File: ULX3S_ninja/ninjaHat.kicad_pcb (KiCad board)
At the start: 2 copper layers, 31.8 x 55.9 mm, 2 parts, among them J1 DVI-HX-107DIP, P1 ULX3S connector (JP1)

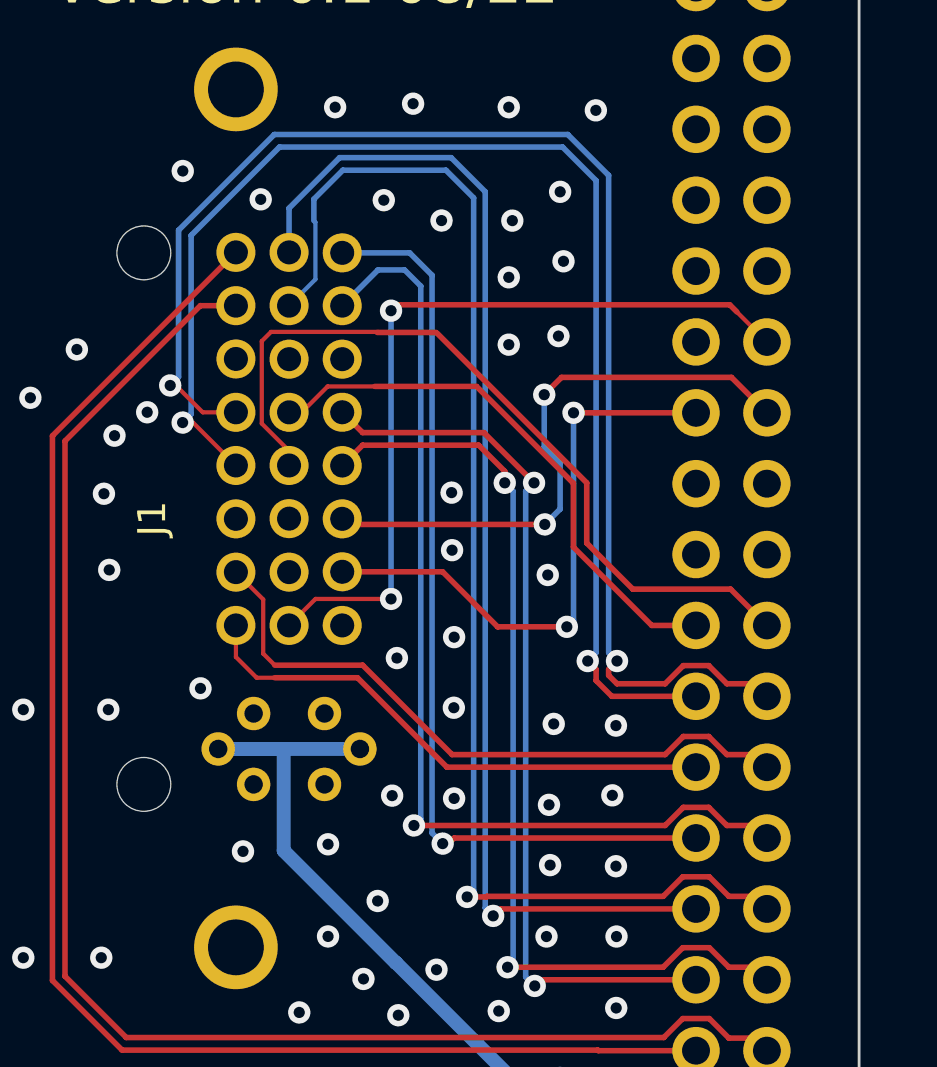
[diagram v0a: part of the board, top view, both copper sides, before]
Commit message: Changed some tracks' width to 0,2mm
was 0,152mm before. Also took a overview over PCB. looks good so far
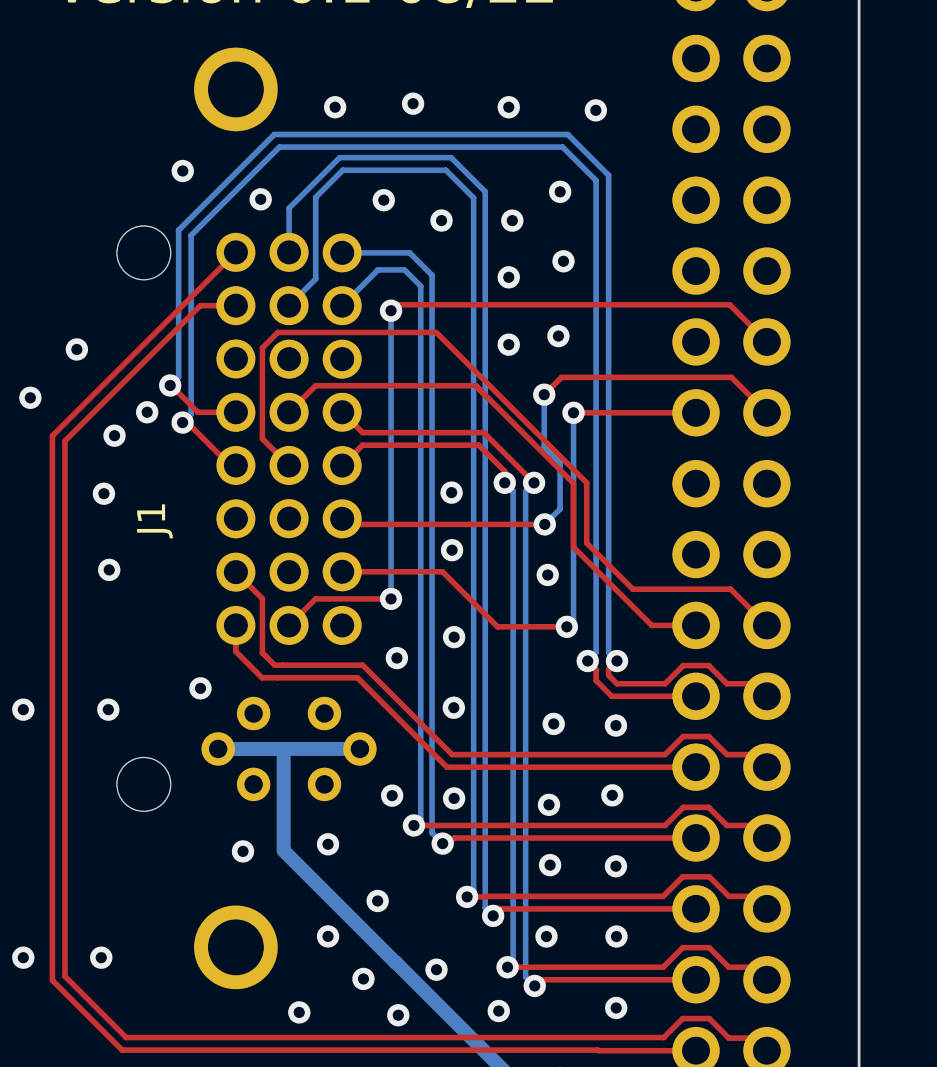
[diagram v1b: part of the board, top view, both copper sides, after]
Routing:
- net /CAM1_SDA: track 28.7 -> 29.9 mm

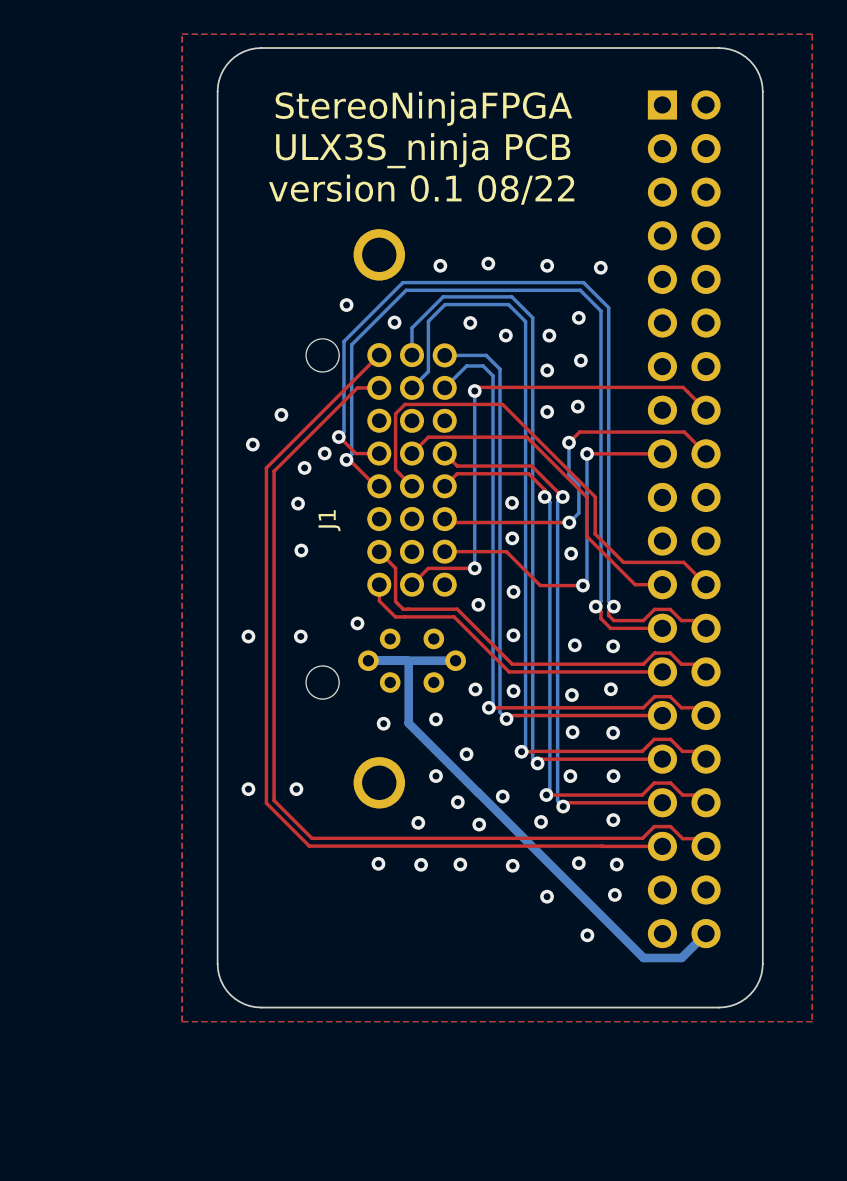
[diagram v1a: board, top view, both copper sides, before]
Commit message: PCB work and pin mapping changed
Did a first PCB layout
changed the pin mapping towards FPGAs four easier routing, schematic need to be rechecked!
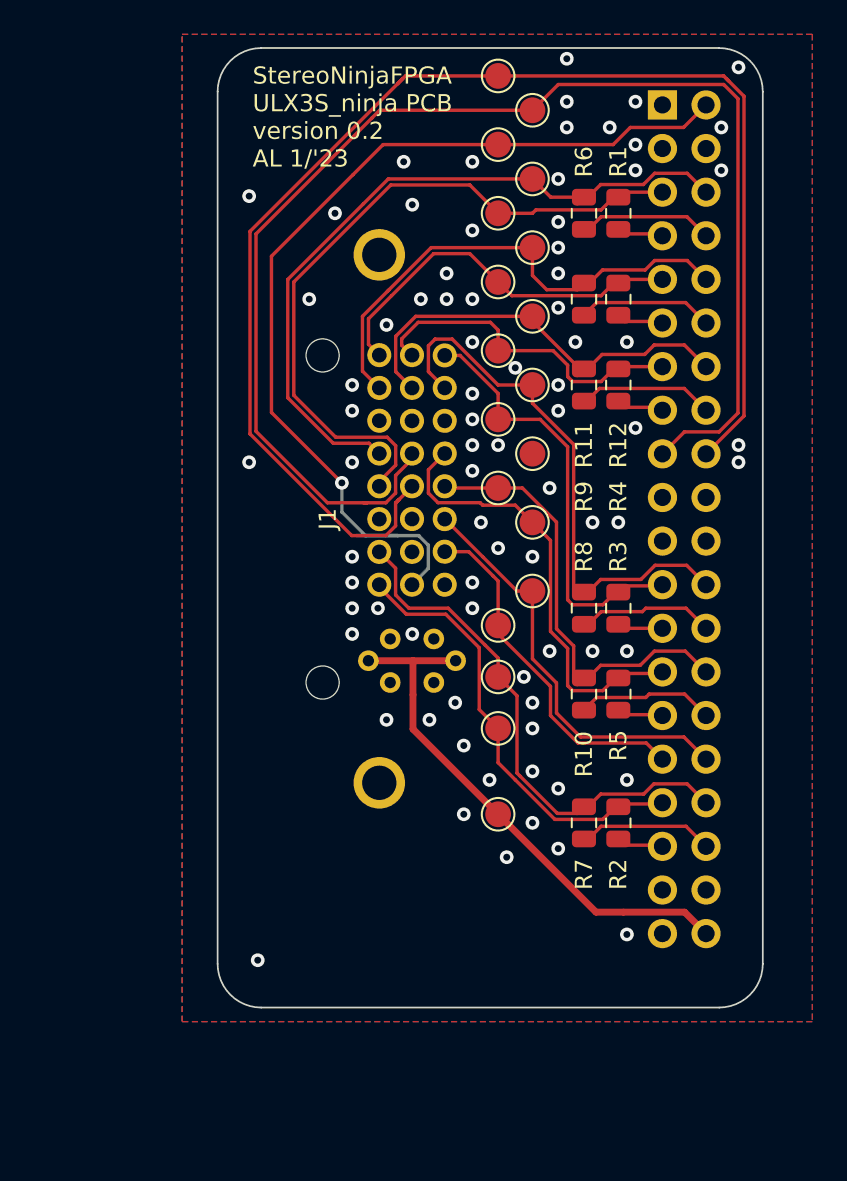
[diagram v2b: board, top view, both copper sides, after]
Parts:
- added R1: 50R, Resistor_SMD:R_0805_2012Metric, F.Cu at (219.0, 103.0)
- added R10: 50R, Resistor_SMD:R_0805_2012Metric, F.Cu at (217.0, 131.0)
- added R11: 50R, Resistor_SMD:R_0805_2012Metric, F.Cu at (217.0, 108.0)
- added R12: 50R, Resistor_SMD:R_0805_2012Metric, F.Cu at (219.0, 108.0)
- added R2: 50R, Resistor_SMD:R_0805_2012Metric, F.Cu at (219.0, 138.5)
- added R3: 50R, Resistor_SMD:R_0805_2012Metric, F.Cu at (219.0, 126.0)
- added R4: 50R, Resistor_SMD:R_0805_2012Metric, F.Cu at (219.0, 113.0)
- added R5: 50R, Resistor_SMD:R_0805_2012Metric, F.Cu at (219.0, 131.0)
- added R6: 50R, Resistor_SMD:R_0805_2012Metric, F.Cu at (217.0, 103.0)
- added R7: 50R, Resistor_SMD:R_0805_2012Metric, F.Cu at (217.0, 138.5)
- added R8: 50R, Resistor_SMD:R_0805_2012Metric, F.Cu at (217.0, 126.0)
- added R9: 50R, Resistor_SMD:R_0805_2012Metric, F.Cu at (217.0, 113.0)
- added TP1: TestPoint, TestPoint:TestPoint_Pad_D1.5mm, F.Cu at (212.0, 107.0)
- added TP10: TestPoint, TestPoint:TestPoint_Pad_D1.5mm, F.Cu at (212.0, 103.0)
- added TP11: TestPoint, TestPoint:TestPoint_Pad_D1.5mm, F.Cu at (212.0, 119.0)
- added TP12: TestPoint, TestPoint:TestPoint_Pad_D1.5mm, F.Cu at (212.0, 95.0)
- added TP13: TestPoint, TestPoint:TestPoint_Pad_D1.5mm, F.Cu at (214.0, 125.0)
- added TP14: TestPoint, TestPoint:TestPoint_Pad_D1.5mm, F.Cu at (212.0, 130.0)
- added TP15: TestPoint, TestPoint:TestPoint_Pad_D1.5mm, F.Cu at (212.0, 127.0)
- added TP16: TestPoint, TestPoint:TestPoint_Pad_D1.5mm, F.Cu at (212.0, 133.0)
- added TP17: TestPoint, TestPoint:TestPoint_Pad_D1.5mm, F.Cu at (212.0, 99.0)
- added TP18: TestPoint, TestPoint:TestPoint_Pad_D1.5mm, F.Cu at (214.0, 117.0)
- added TP19: TestPoint, TestPoint:TestPoint_Pad_D1.5mm, F.Cu at (212.0, 138.0)
- added TP2: TestPoint, TestPoint:TestPoint_Pad_D1.5mm, F.Cu at (212.0, 115.0)
- added TP3: TestPoint, TestPoint:TestPoint_Pad_D1.5mm, F.Cu at (212.0, 111.0)
- added TP4: TestPoint, TestPoint:TestPoint_Pad_D1.5mm, F.Cu at (214.0, 105.0)
- added TP5: TestPoint, TestPoint:TestPoint_Pad_D1.5mm, F.Cu at (214.0, 113.0)
- added TP6: TestPoint, TestPoint:TestPoint_Pad_D1.5mm, F.Cu at (214.0, 109.0)
- added TP7: TestPoint, TestPoint:TestPoint_Pad_D1.5mm, F.Cu at (214.0, 101.0)
- added TP8: TestPoint, TestPoint:TestPoint_Pad_D1.5mm, F.Cu at (214.0, 121.0)
- added TP9: TestPoint, TestPoint:TestPoint_Pad_D1.5mm, F.Cu at (214.0, 97.0)
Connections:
- net /CAM_3V3 renamed +3V3
- P1 pad 10: unconnected-(P1-Pad10) -> /CAM1_CLK_N
- P1 pad 11: unconnected-(P1-Pad11) -> /CAM1_CLK_R_P
- P1 pad 12: unconnected-(P1-Pad12) -> /CAM1_CLK_R_N
- P1 pad 13: unconnected-(P1-Pad13) -> /CAM1_D1_P
- P1 pad 14: unconnected-(P1-Pad14) -> /CAM1_D1_N
- P1 pad 15: unconnected-(P1-Pad15) -> /CAM1_D1__R_P
- P1 pad 16: /CAM_GPIO -> /CAM1_D1_R_N
- P1 pad 17: /CAM0_SCL -> /CAM1_SCL
- P1 pad 18: /CAM0_SDA -> /CAM1_SDA
- P1 pad 2: unconnected-(P1-Pad2) -> /CAM_GPIO
- P1 pad 23: /CAM1_SCL -> /CAM1_D0_P
- P1 pad 24: /CAM1_SDA -> /CAM1_D0_N
- P1 pad 25: /CAM0_D0_P -> /CAM1_D0_R_P
- P1 pad 26: /CAM0_D0_N -> /CAM1_D0_R_N
- P1 pad 27: /CAM0_D1_P -> /CAM0_CLK_P
- P1 pad 28: /CAM0_D1_N -> /CAM0_CLK_N
- P1 pad 29: /CAM1_D0_P -> /CAM0_CLK_R_P
- P1 pad 30: /CAM1_D0_N -> /CAM0_CLK_R_N
- P1 pad 31: /CAM1_D1_P -> /CAM0_SCL
- P1 pad 32: /CAM1_D1_N -> /CAM0_SDA
- P1 pad 33: /CAM0_CLK_P -> /CAM0_D1_P
- P1 pad 34: /CAM0_CLK_N -> /CAM0_D1_N
- P1 pad 35: /CAM1_CLK_P -> /CAM0_D1_R_P
- P1 pad 36: /CAM1_CLK_N -> /CAM0_D1_R_N
- P1 pad 5: unconnected-(P1-Pad5) -> /CAM0_D0_P
- P1 pad 6: unconnected-(P1-Pad6) -> /CAM0_D0_N
- P1 pad 7: unconnected-(P1-Pad7) -> /CAM0_D0_R_P
- P1 pad 8: unconnected-(P1-Pad8) -> /CAM0_D0_R_N
- P1 pad 9: unconnected-(P1-Pad9) -> /CAM1_CLK_P
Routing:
- net /CAM1_SCL: track 20.2 -> 80.2 mm
- net /CAM1_SDA: track 29.9 -> 81.3 mm
- net /CAM1_CLK_P: track 52.9 -> 23.3 mm
- net /CAM_GPIO: track 28.5 -> 56.5 mm, vias 2 -> 1
- net /CAM1_CLK_N: track 54.1 -> 30.5 mm
- net /CAM1_D1_P: track 43.3 -> 19.7 mm, vias 1 -> 0
- net /CAM1_D1_N: track 47.4 -> 24.8 mm, vias 1 -> 0
- net /CAM1_D0_P: track 33.2 -> 23.6 mm, vias 1 -> 0
- net /CAM0_CLK_N: track 34.6 -> 25.6 mm, vias 2 -> 0
- net /CAM1_CLK_R_N: track 0.00 -> 8.27 mm
- net /CAM0_CLK_R_N: track 0.00 -> 8.02 mm
- net /CAM1_D0_R_N: track 0.00 -> 7.98 mm
- net /CAM1_D1_R_N: track 0.00 -> 7.94 mm
- net /CAM0_D1_R_N: track 0.00 -> 7.90 mm
- net /CAM0_D0_R_N: track 0.00 -> 7.88 mm
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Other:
- board text added: "StereoNinjaFPGA ULX3S_ninja PCB version 0.2 AL 1/'23"
- board text removed: "StereoNinjaFPGA ULX3S_ninja PCB version 0.1 08/22"

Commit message: Pin Mapping changed again
Please check
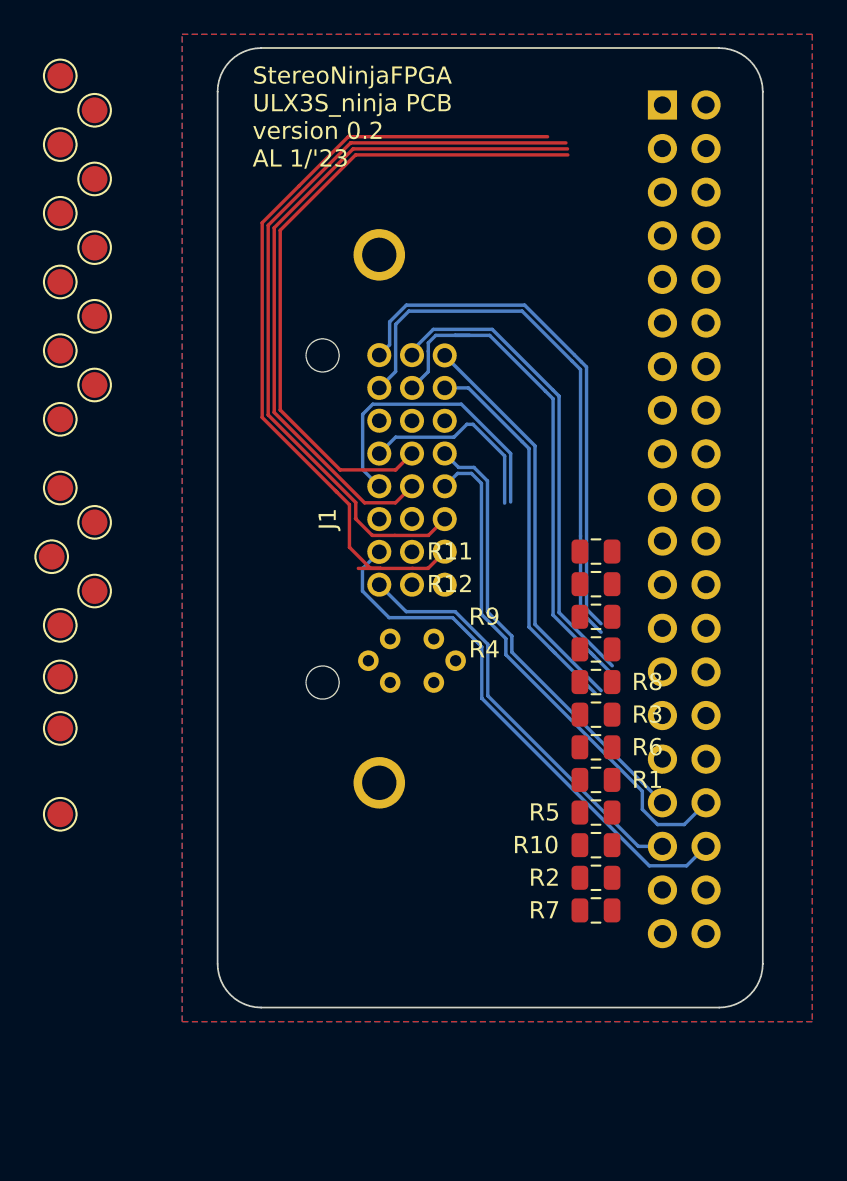
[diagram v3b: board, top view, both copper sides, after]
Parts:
- moved R1 33.0 mm to (217.7, 136.0), turned to 180 degrees
- moved R6 31.1 mm to (217.7, 134.1), turned to 0 degrees
- moved TP18 28.6 mm to (186.0, 123.0)
- moved TP1 25.5 mm to (186.5, 107.0)
- moved TP10 25.5 mm to (186.5, 103.0)
- moved TP11 25.5 mm to (186.5, 119.0)
- moved TP12 25.5 mm to (186.5, 95.0)
- moved TP13 25.5 mm to (188.5, 125.0)
- moved TP14 25.5 mm to (186.5, 130.0)
- moved TP15 25.5 mm to (186.5, 127.0)
- moved TP16 25.5 mm to (186.5, 133.0)
- moved TP17 25.5 mm to (186.5, 99.0)
- moved TP19 25.5 mm to (186.5, 138.0)
- moved TP2 25.5 mm to (186.5, 115.0)
- moved TP3 25.5 mm to (186.5, 111.0)
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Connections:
- P1 pad 10: /CAM1_CLK_N -> /CAM0_D1_R_N
- P1 pad 11: /CAM1_CLK_R_P -> /CAM0_CLK_R_P
- P1 pad 12: /CAM1_CLK_R_N -> /CAM0_CLK_R_N
- P1 pad 13: /CAM1_D1_P -> /CAM0_D0_R_P
- P1 pad 14: /CAM1_D1_N -> /CAM0_D0_R_N
- P1 pad 15: /CAM1_D1__R_P -> /CAM1_D0_R_P
- P1 pad 16: /CAM1_D1_R_N -> /CAM1_D0_R_N
- P1 pad 17: /CAM1_SCL -> /CAM1_D1__R_P
- P1 pad 18: /CAM1_SDA -> /CAM1_D1_R_N
- P1 pad 23: /CAM1_D0_P -> /CAM1_CLK_R_P
- P1 pad 24: /CAM1_D0_N -> /CAM1_CLK_R_N
- P1 pad 25: /CAM1_D0_R_P -> /CAM1_CLK_P
- P1 pad 26: /CAM1_D0_R_N -> /CAM1_CLK_N
- P1 pad 27: /CAM0_CLK_P -> /CAM1_D1_P
- P1 pad 28: /CAM0_CLK_N -> /CAM1_D1_N
- P1 pad 29: /CAM0_CLK_R_P -> /CAM1_D0_P
- P1 pad 30: /CAM0_CLK_R_N -> /CAM1_D0_N
- P1 pad 31: /CAM0_SCL -> /CAM0_D0_P
- P1 pad 32: /CAM0_SDA -> /CAM0_D0_N
- P1 pad 33: /CAM0_D1_P -> /CAM0_CLK_P
- P1 pad 34: /CAM0_D1_N -> /CAM0_CLK_N
- P1 pad 35: /CAM0_D1_R_P -> /CAM0_D1_P
- P1 pad 36: /CAM0_D1_R_N -> /CAM0_D1_N
- P1 pad 5: /CAM0_D0_P -> /CAM0_SCL
- P1 pad 6: /CAM0_D0_N -> /CAM0_SDA
- P1 pad 7: /CAM0_D0_R_P -> /CAM1_SCL
- P1 pad 8: /CAM0_D0_R_N -> /CAM1_SDA
- P1 pad 9: /CAM1_CLK_P -> /CAM0_D1_R_P
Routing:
- net /CAM_GPIO: track 56.5 -> 0.00 mm, vias 1 -> 0
- net /CAM1_SCL: track 80.2 -> 38.5 mm
- net /CAM1_SDA: track 81.3 -> 40.3 mm
- net /CAM0_D0_N: track 42.9 -> 11.5 mm
- net +3V3: track 31.1 -> 0.00 mm
- net /CAM0_SCL: track 20.5 -> 47.6 mm
- net /CAM0_D0_P: track 42.0 -> 17.5 mm
- net /CAM0_SDA: track 24.3 -> 44.5 mm
- net /CAM1_D1_P: track 19.7 -> 28.4 mm
- net /CAM1_D0_N: track 31.2 -> 22.6 mm
- net /CAM1_CLK_R_N: track 8.27 -> 0.00 mm
- net /CAM0_CLK_R_N: track 8.02 -> 0.00 mm
- net /CAM1_D0_R_N: track 7.98 -> 0.00 mm
- net /CAM1_D1_R_N: track 7.94 -> 0.00 mm
- net /CAM0_D1_R_N: track 7.90 -> 0.00 mm
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
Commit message: Layout finished
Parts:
- removed TP1, TP10, TP11, TP14, TP16, TP2, TP3, TP4, TP5, TP6, TP7, TP8: TestPoint, TestPoint:TestPoint_Pad_D1.5mm
- moved TP15 42.1 mm to (217.0, 98.0)
- moved TP13 37.3 mm to (217.0, 101.0)
- moved TP12 31.8 mm to (217.0, 104.0)
- moved TP18 31.2 mm to (210.0, 143.0)
- moved TP17 30.8 mm to (217.0, 95.0)
- moved TP9 30.2 mm to (217.0, 107.0)
- moved TP19 24.8 mm to (210.0, 146.0)
- moved R10 1.90 mm to (217.7, 137.9)
- moved R2 1.90 mm to (217.7, 143.6)
- moved R5 1.90 mm to (217.7, 139.8)
- moved R7 1.90 mm to (217.7, 141.7)
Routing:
- net /CAM_GPIO: track 0.00 -> 57.2 mm
- net GND: track 0.00 -> 45.4 mm, vias 0 -> 81
- net /CAM0_D1_R_N: track 0.00 -> 42.7 mm
- net /CAM0_D1_R_P: track 0.00 -> 42.0 mm
- net +3V3: track 0.00 -> 40.0 mm
- net /CAM0_CLK_R_N: track 0.00 -> 36.7 mm
- net /CAM0_CLK_R_P: track 0.00 -> 36.0 mm
- net /CAM0_D0_R_N: track 0.00 -> 30.7 mm
- net /CAM0_D0_N: track 11.5 -> 41.6 mm
- net /CAM0_D0_R_P: track 0.00 -> 29.9 mm
- net /CAM0_D0_P: track 17.5 -> 41.1 mm
- net /CAM1_D0_R_N: track 0.00 -> 21.9 mm
- net /CAM1_D0_R_P: track 0.00 -> 21.2 mm
- net /CAM0_D1_P: track 24.6 -> 42.3 mm
- net /CAM0_D1_N: track 31.5 -> 49.1 mm
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
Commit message: added pinheaders for D0 D1 and CLK (cam0 only) for debugging
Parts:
- added J_CLK0: Conn_01x03_Male, Connector_PinHeader_1.27mm:PinHeader_1x03_P1.27mm_Vertical, F.Cu at (206.3, 142.5)
- added J_D0: Conn_01x03_Male, Connector_PinHeader_1.27mm:PinHeader_1x03_P1.27mm_Vertical, F.Cu at (211.2, 142.5)
- added J_D1: Conn_01x03_Male, Connector_PinHeader_1.27mm:PinHeader_1x03_P1.27mm_Vertical, F.Cu at (201.8, 142.5)
- moved TP18 12.3 mm to (197.7, 144.0)
- moved TP19 12.3 mm to (197.7, 146.7)
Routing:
- net /CAM0_CLK_P: track 31.8 -> 57.3 mm
- net /CAM0_CLK_N: track 37.3 -> 62.2 mm
- net +3V3: track 40.0 -> 62.1 mm
- net /CAM0_D0_P: track 41.1 -> 63.1 mm
- net /CAM0_D0_N: track 41.6 -> 62.9 mm
- net GND: track 45.4 -> 60.2 mm, vias 81 -> 101
- net /CAM0_D1_P: track 42.3 -> 56.0 mm
- net /CAM0_D1_N: track 49.1 -> 62.8 mm
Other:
- board text added: "+ -"
- board text added: "CLK"
- board text added: "D0"
- board text added: "D1"

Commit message: added 2nd gnd pin to debugging connectors
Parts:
- J_CLK0, J_D0, J_D1: value Conn_01x03_Male -> Conn_01x04_Male; footprint Connector_PinHeader_1.27mm:PinHeader_1x03_P1.27mm_Vertical -> Connector_PinHeader_1.27mm:PinHeader_1x04_P1.27mm_Vertical
- moved J_D1 0.05 mm to (201.8, 142.5)
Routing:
- net /CAM0_CLK_P: track 57.3 -> 58.2 mm
- net /CAM0_CLK_N: track 62.2 -> 63.1 mm
- net /CAM0_D1_N: track 62.8 -> 63.5 mm
- net /CAM0_D1_P: track 56.0 -> 56.6 mm
- net GND: vias 101 -> 100

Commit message: fixed pin header footprint
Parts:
- J_CLK0, J_D0, J_D1: footprint Connector_PinHeader_1.27mm:PinHeader_1x04_P1.27mm_Vertical -> Connector_PinHeader_2.54mm:PinHeader_1x04_P2.54mm_Vertical
- moved TP18 3.80 mm to (197.7, 147.8)
- moved TP19 3.80 mm to (197.7, 150.5)
- moved J_CLK0 2.94 mm to (206.0, 145.4)
- moved J_D0 2.94 mm to (210.9, 145.4)
- moved J_D1 2.94 mm to (201.5, 145.4)
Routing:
- net /CAM0_CLK_N: track 63.1 -> 81.2 mm
- net /CAM0_CLK_P: track 58.2 -> 75.9 mm
- net /CAM0_D1_P: track 56.6 -> 72.9 mm
- net /CAM0_D1_N: track 63.5 -> 79.3 mm
- net +3V3: track 62.1 -> 77.3 mm
- net /CAM0_D0_N: track 62.9 -> 74.9 mm
- net /CAM0_D0_P: track 63.1 -> 74.7 mm
- net GND: track 60.2 -> 64.1 mm, vias 100 -> 112
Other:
- board size 31.8 x 55.9 mm -> 31.8 x 63.8 mm
- board text added: "StereoNinjaFPGA ULX3S_ninja PCB version 0.3 AL+AK 2/'23"
- board text removed: "StereoNinjaFPGA ULX3S_ninja PCB version 0.2 AL 1/'23"
